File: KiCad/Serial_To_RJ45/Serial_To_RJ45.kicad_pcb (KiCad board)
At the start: 2 copper layers, 21.7 x 22.3 mm, 3 parts, among them J1 RJE561881410, J2 Serial IDC Header

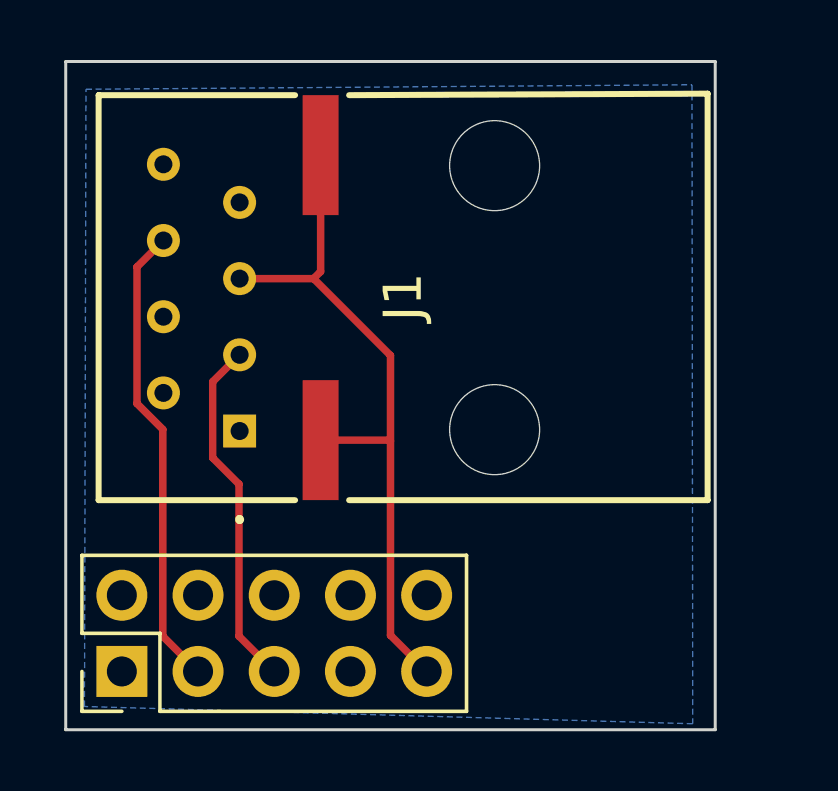
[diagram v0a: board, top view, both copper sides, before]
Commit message: Added Switch for RX TX
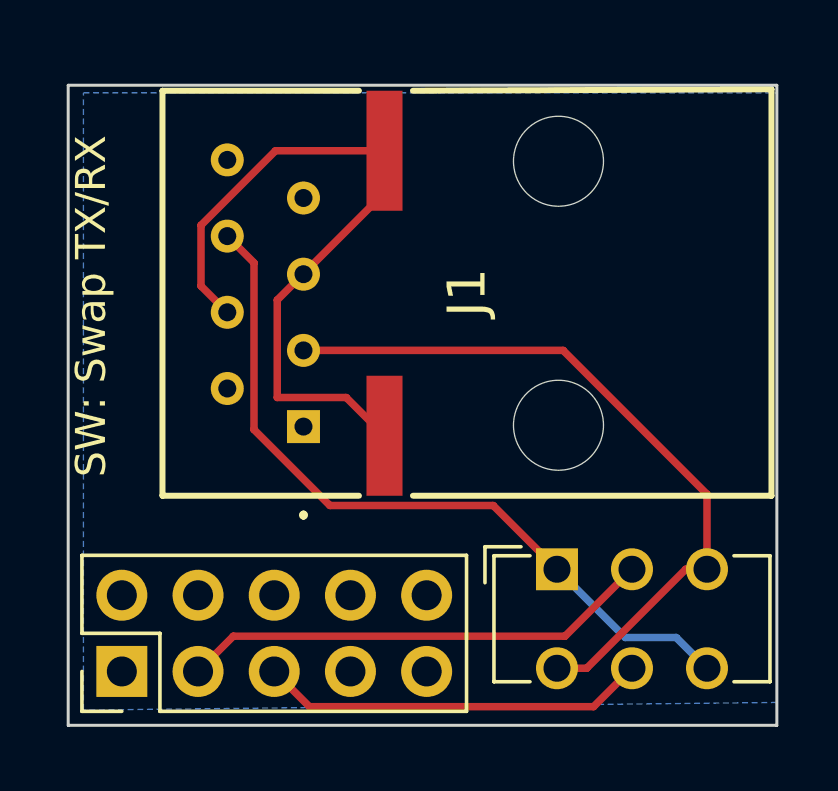
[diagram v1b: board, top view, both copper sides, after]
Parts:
- added SW: Swap TX/RX: SW_DPDT_x2, Button_Switch_THT:SW_CuK_JS202011CQN_DPDT_Straight, F.Cu at (208.8, 118.8)
- moved J1 2.13 mm to (200.4, 114.0)
- moved REF** 1.78 mm to (211.8, 109.0)
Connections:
- J2 pad 3: /RXD -> Net-(J2-Pin_3)
- J2 pad 5: /TXD -> Net-(J2-Pin_5)
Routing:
- net Net-(J2-Pin_3): track 0.00 -> 15.9 mm
- net Net-(J2-Pin_5): track 0.00 -> 12.9 mm
- net /TXD: track 11.8 -> 24.3 mm
- net /RXD: track 15.6 -> 25.2 mm
- net GND: track 23.7 -> 24.2 mm
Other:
- board size 21.7 x 22.3 mm -> 23.6 x 21.3 mm
